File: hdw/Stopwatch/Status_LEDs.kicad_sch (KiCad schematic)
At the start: 20 parts

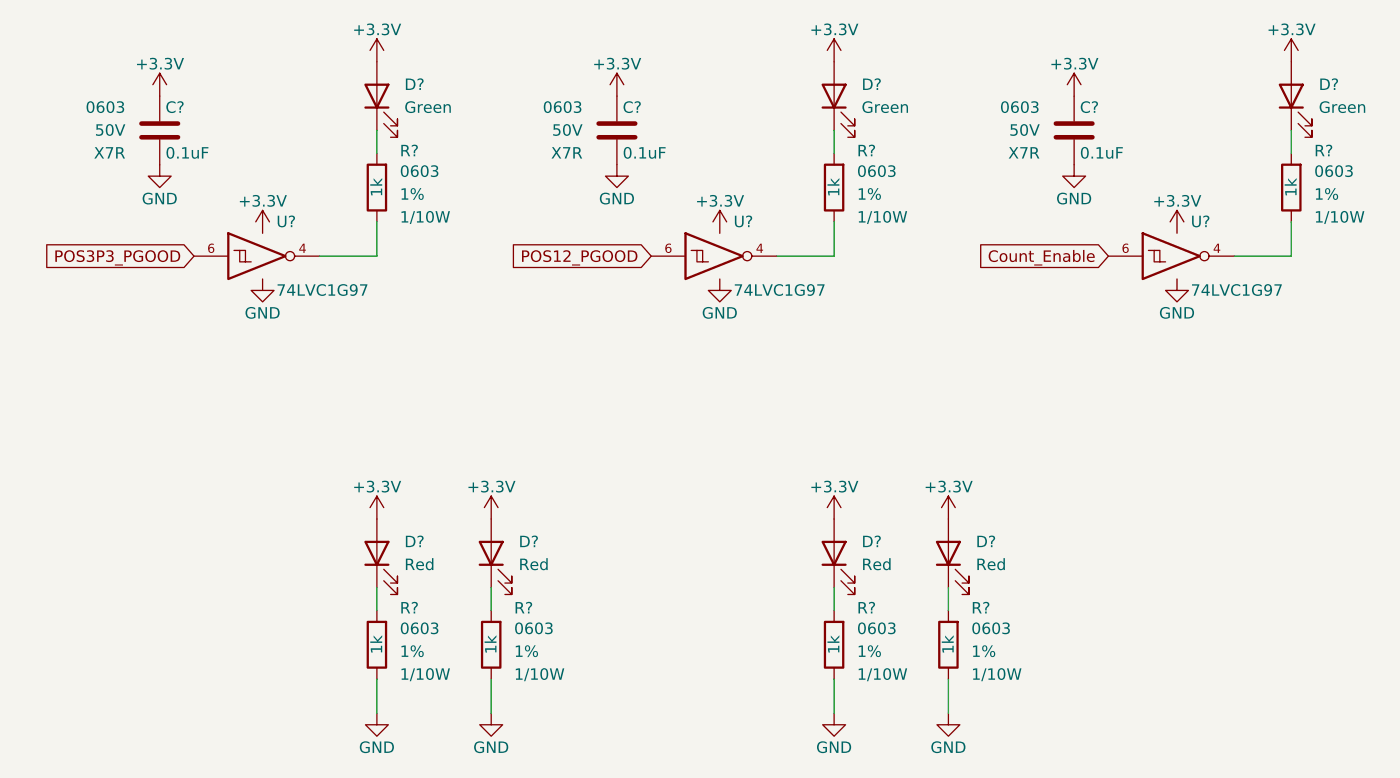
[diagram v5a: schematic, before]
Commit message: Assigned some digikey pns
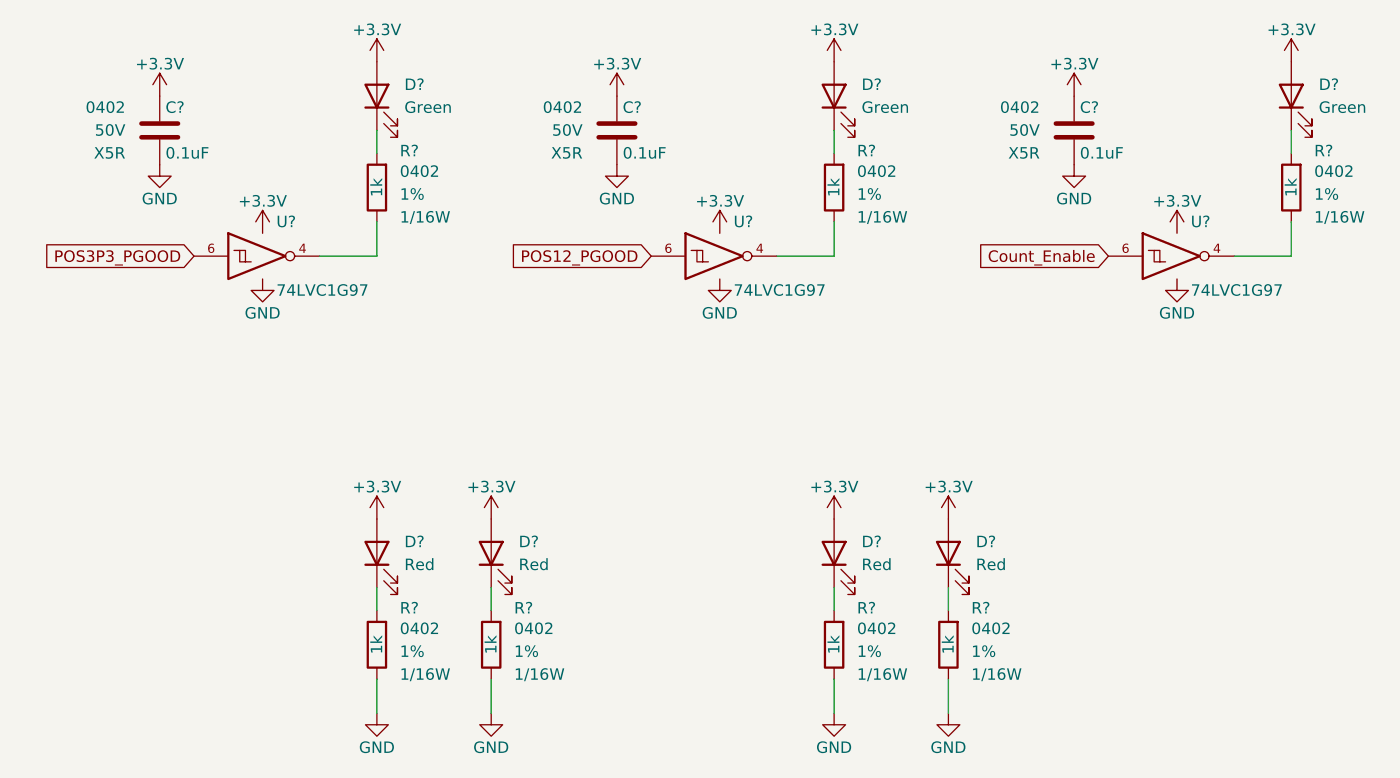
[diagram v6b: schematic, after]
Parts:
- C? (x3): footprint Capacitors_SMD:C_0603 -> Capacitors_SMD:C_0402; Dielectric X7R -> X5R; Digi-Key PN 311-1344-1-ND -> 490-10697-1-ND; display_footprint 0603 -> 0402
- D? (x3): footprint LEDs:LED_0603 -> LEDs:LED_0402; Digi-Key PN 160-1446-1-ND -> 754-1101-1-ND
- D? (x4): footprint LEDs:LED_0603 -> LEDs:LED_0402; Digi-Key PN (none) -> 754-1104-1-ND
- R? (x7): footprint Resistors_SMD:R_0603 -> Resistors_SMD:R_0402; Digi-Key PN RHM1.0KDCT-ND -> RMCF0402FT1K00CT-ND; Wattage 1/10W -> 1/16W; display_footprint 0603 -> 0402
- U? (x3): footprint Package_TO_SOT_SMD:SOT-363_SC-70-6 -> (none); Digi-Key PN (none) -> 296-29875-1-ND

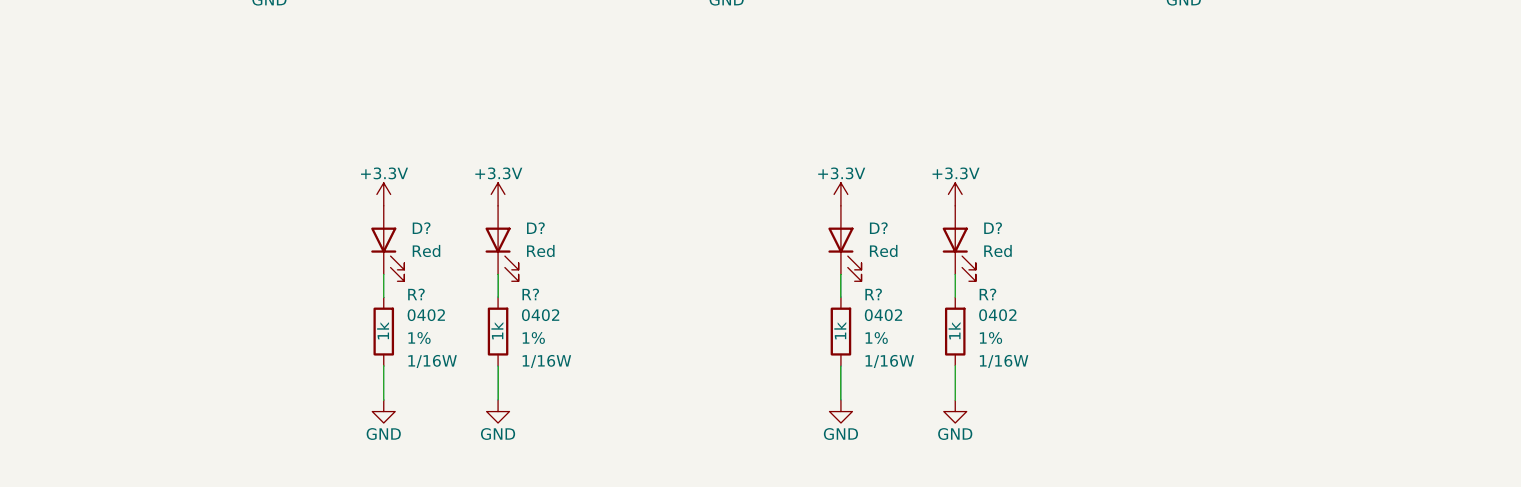
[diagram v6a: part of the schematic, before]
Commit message: added ability to turn off colons
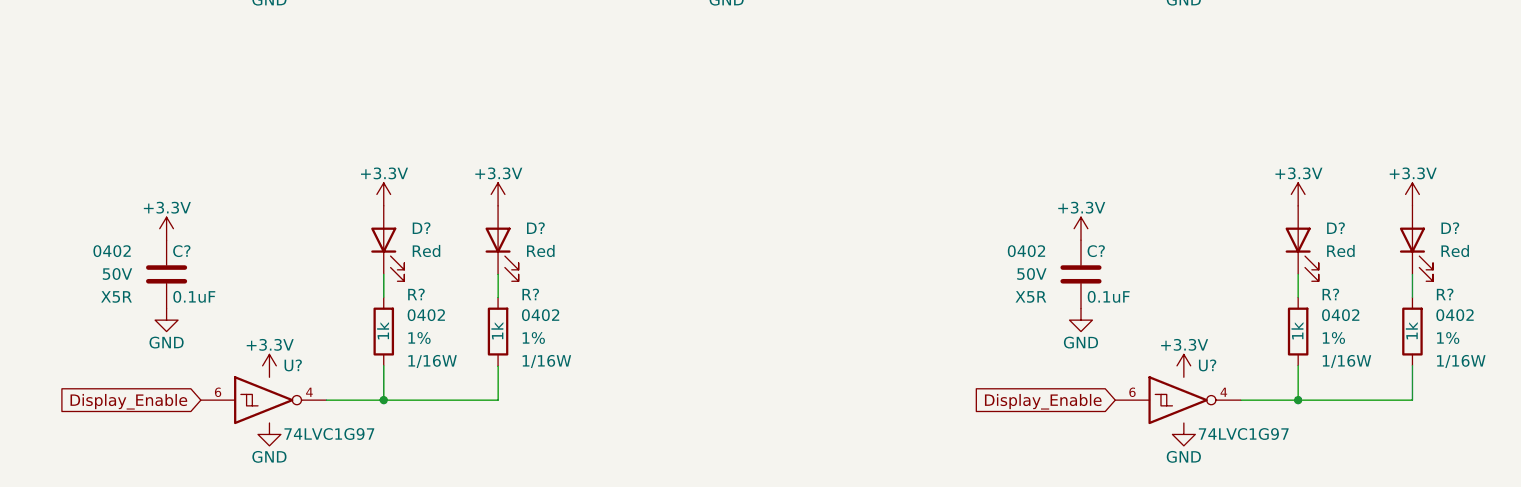
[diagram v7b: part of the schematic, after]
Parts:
- added C? (x2): 0.1uF, Capacitors_SMD:C_0402, symbol Custom_Library:C_Custom
- added U? (x2): 74LVC1G97, symbol Custom Library:74LVC1G97_Power_NOT
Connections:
- net +3V3: now also C?.1, C?.1, U?.1 (VCC), U?.1 (VCC), U?.5 (VCC), U?.5 (VCC)
- net GND: now also C?.2, C?.2, U?.2 (GND), U?.2 (GND), U?.3 (GND), U?.3 (GND); no longer R?.2, R?.2, R?.2, R?.2
- new net: R?.2, R?.2, U?.4 (x2)
- new net Display_Enable: U?.6, U?.6
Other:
- moved on the sheet: D?, R?

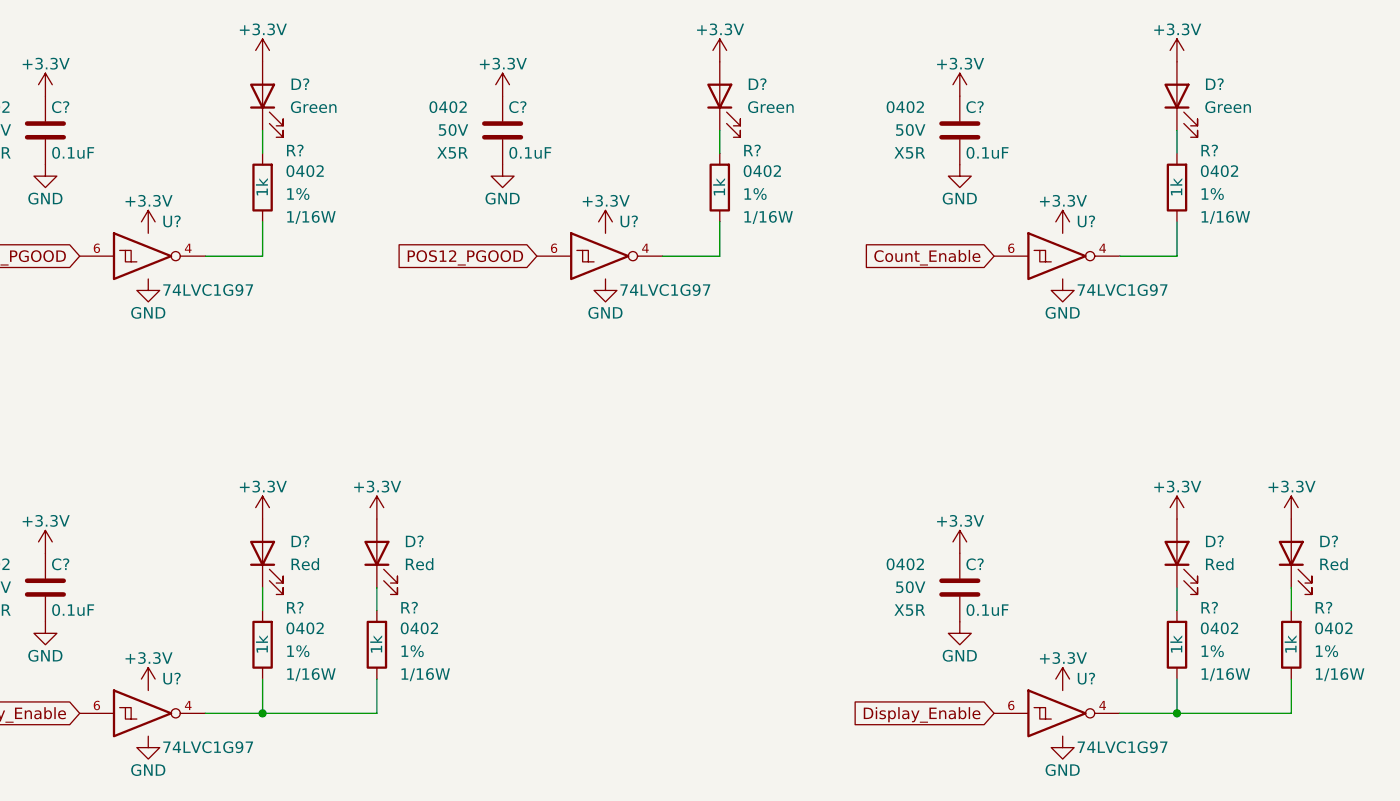
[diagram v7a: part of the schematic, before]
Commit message: added proper power sequencing, discharge
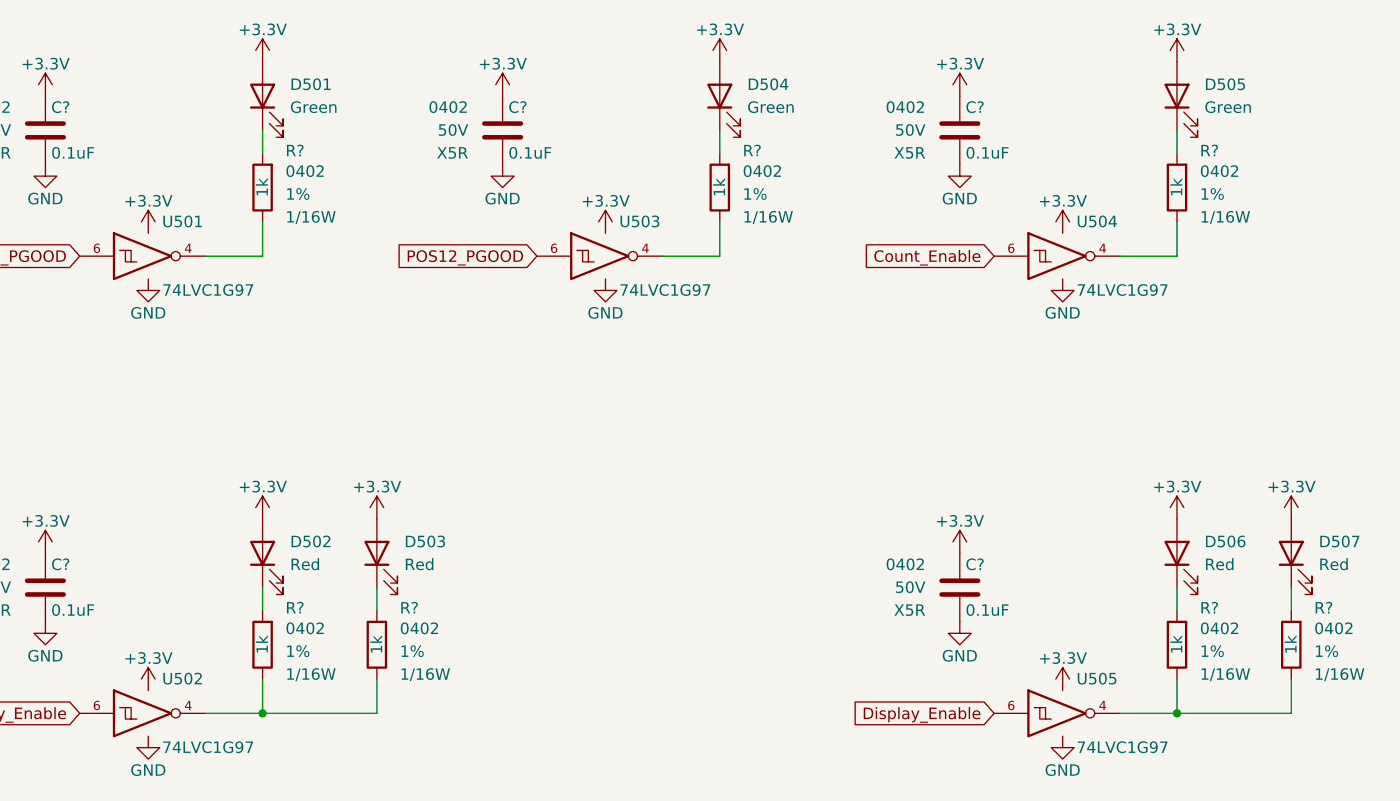
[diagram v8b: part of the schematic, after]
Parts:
- U501, U502, U503, U504, U505: renamed from U?; footprint (none) -> Package_SON:Fairchild_MicroPak2-6_1.0x1.0mm_P0.35mm
- gave numbers to parts that had none: 7
